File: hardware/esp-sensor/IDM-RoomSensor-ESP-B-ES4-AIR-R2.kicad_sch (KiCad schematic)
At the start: 115 parts, among them J1 MX205R / 43 TEMP / 42 +6-32V 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, J2 1-2834011-4 / RS485 A / B / C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, J3 TYPE-C-31-M-12, J4 EXPANSION / LED_EN / RELAY, J5 MX205R PUSH-IN / 3V3 / 1-WIRE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, J6 MX205R PUSH-IN / 3V3 / 1-WIRE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, J7 MX205R PUSH-IN / CONTACT1 / C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, J8 MX205R PUSH-IN / 0-10V IN / G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, J9 MX205R PUSH-IN / COM / NO / NC, K1 HFD4/5 5V DPDT signal relay, Q1 2N7002 60V VIN LED switch, Q2 2N7002 relay driver, SW1 RESET, SW2 BOOT, SW3 RS485 TERM ON/OFF, SW4 SERVICE / IDENTIFY, U1 LMR36510ADDAR 24V-to-5V, U10 BMP390, U11 AP2112K-3.3TRG1 AIR RAIL, U2 AP2112K-3.3TRG1, U3 ESP32-C6-WROOM-1-N16 (pins pe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, U4 SHT45-AD1B-R2, U5 MCP4725A0T-E/CH, U6 OPA197IDBVR, U7 CA-IS3092W, U8 SCD41-D-R1, U9 SGP41-D-R4

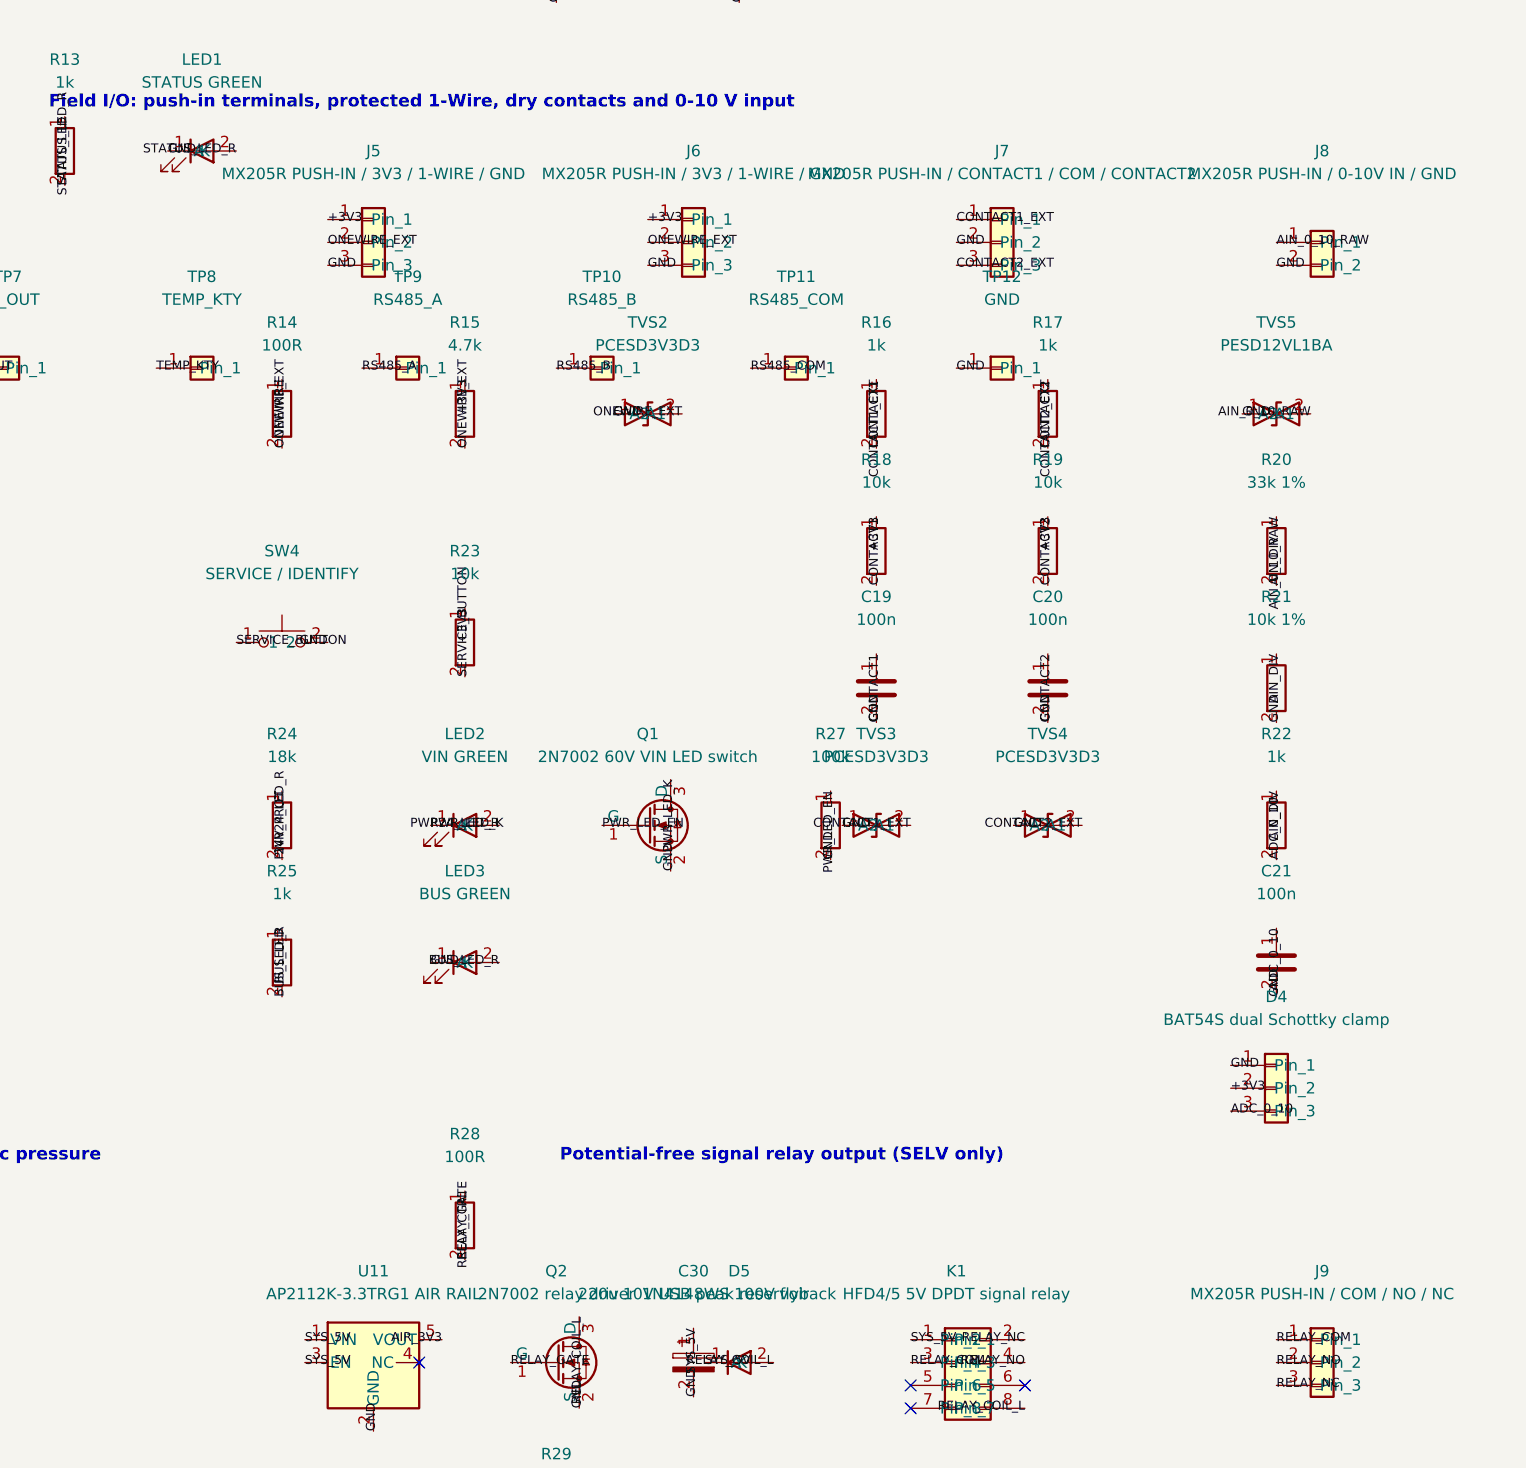
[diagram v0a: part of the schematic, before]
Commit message: Replace unavailable B-ES4 R2 terminals
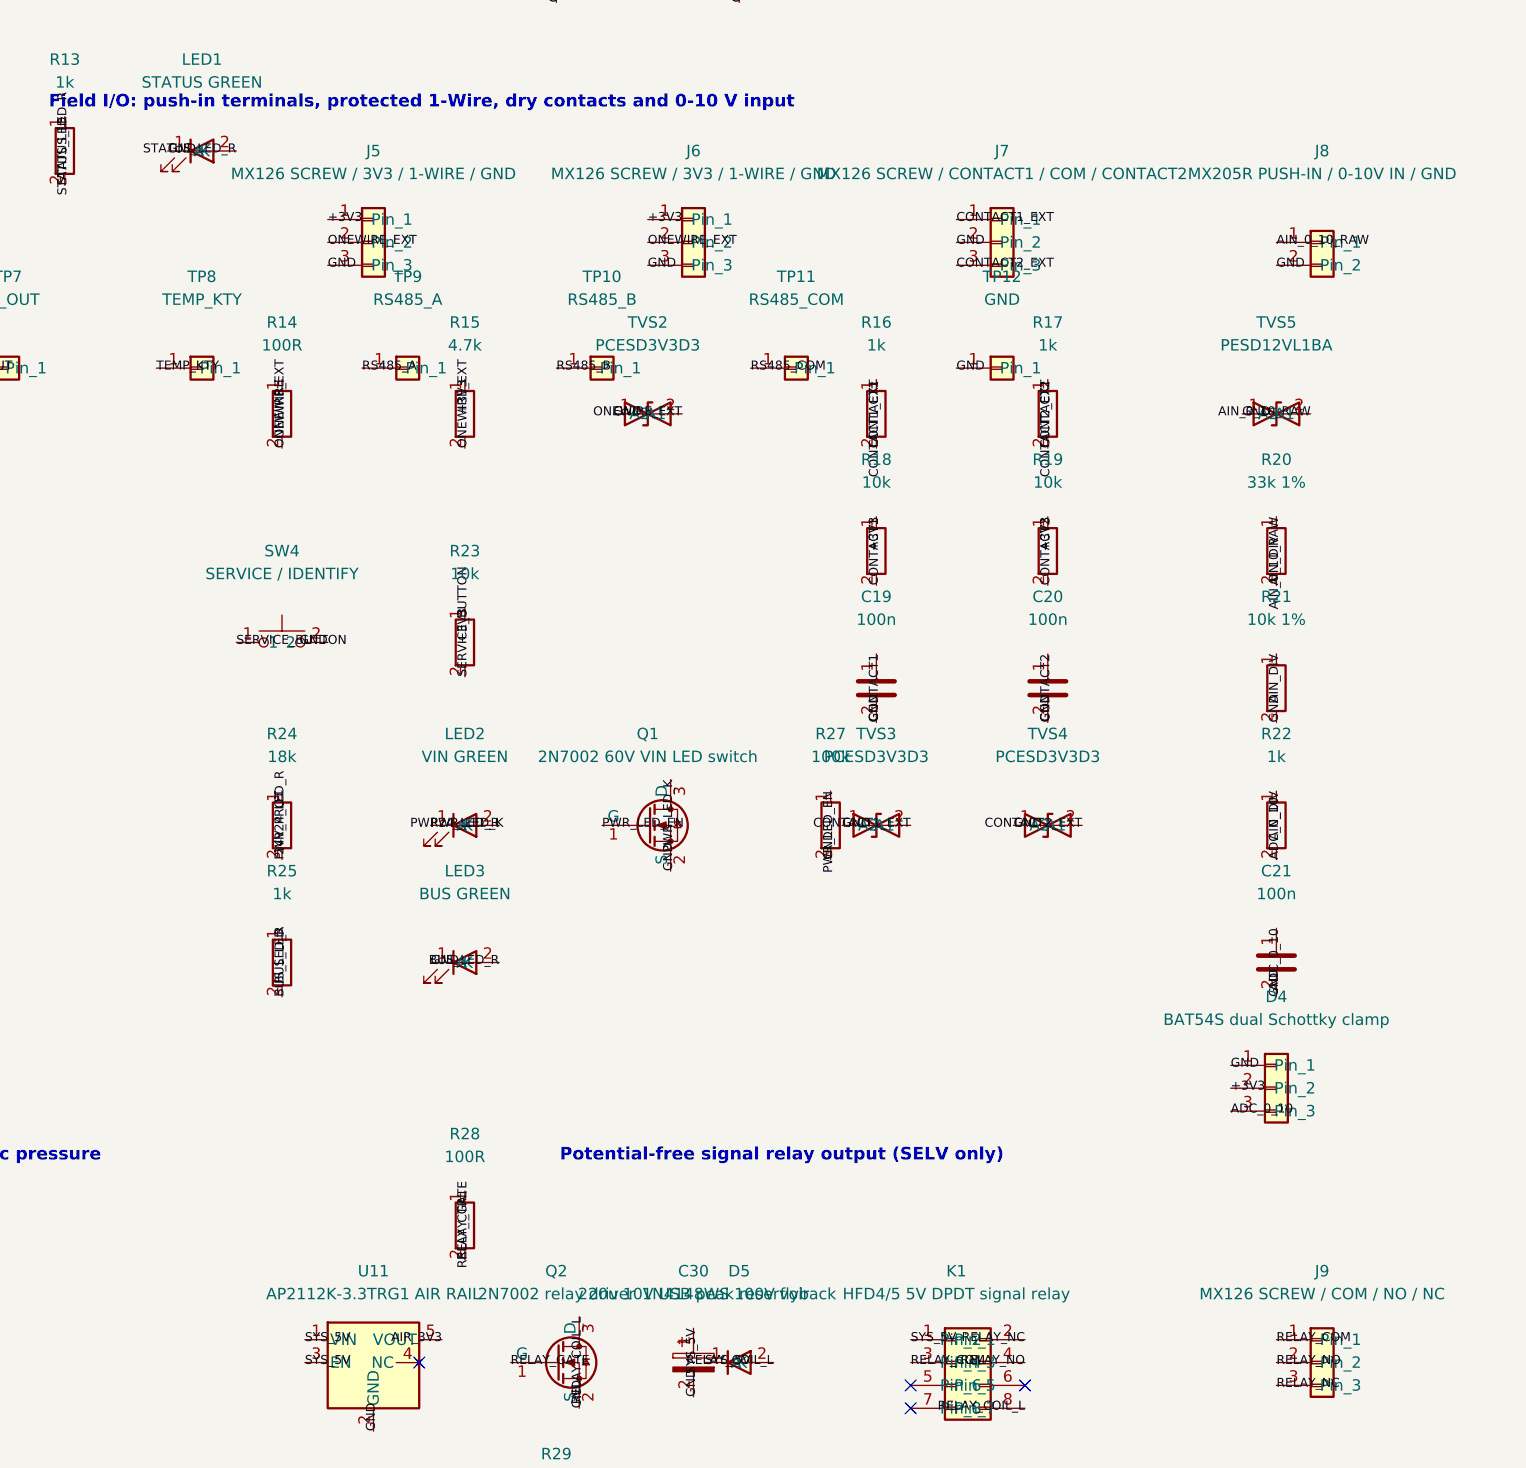
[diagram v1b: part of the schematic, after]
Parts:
- J5, J6: value MX205R PUSH-IN / 3V3 / 1-WIRE / GND -> MX126 SCREW / 3V3 / 1-WIRE / GND
- J7: value MX205R PUSH-IN / CONTACT1 / COM / CONTACT2 -> MX126 SCREW / CONTACT1 / COM / CONTACT2
- J9: value MX205R PUSH-IN / COM / NO / NC -> MX126 SCREW / COM / NO / NC
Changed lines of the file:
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@@
       (effects (font (size 1.27 1.27)))
     )
-    (property "Value" "MX205R PUSH-IN / 3V3 / 1-WIRE / GND" (at 214.63 182.88 0)
+    (property "Value" "MX126 SCREW / 3V3 / 1-WIRE / GND" (at 214.63 182.88 0)
       (effects (font (size 1.27 1.27)))
     )
@@
       (effects (font (size 1.27 1.27)) hide)
     )
-    (property "Datasheet" "https://www.lcsc.com/product-detail/C7471335.html" (at 214.63 185.42000000000002 0)
+    (property "Datasheet" "https://www.lcsc.com/product-detail/C5188435.html" (at 214.63 185.42000000000002 0)
       (effects (font (size 1.27 1.27)) hide)
     )
@@
       (effects (font (size 1.27 1.27)))
     )
-    (property "Value" "MX205R PUSH-IN / 3V3 / 1-WIRE / GND" (at 250.19 182.88 0)
+    (property "Value" "MX126 SCREW / 3V3 / 1-WIRE / GND" (at 250.19 182.88 0)
       (effects (font (size 1.27 1.27)))
     )
@@
       (effects (font (size 1.27 1.27)) hide)
     )
-    (property "Datasheet" "https://www.lcsc.com/product-detail/C7471335.html" (at 250.19 185.42000000000002 0)
+    (property "Datasheet" "https://www.lcsc.com/product-detail/C5188435.html" (at 250.19 185.42000000000002 0)
       (effects (font (size 1.27 1.27)) hide)
     )
@@
       (effects (font (size 1.27 1.27)))
     )
-    (property "Value" "MX205R PUSH-IN / CONTACT1 / COM / CONTACT2" (at 284.48 182.88 0)
+    (property "Value" "MX126 SCREW / CONTACT1 / COM / CONTACT2" (at 284.48 182.88 0)
       (effects (font (size 1.27 1.27)))
     )
@@
       (effects (font (size 1.27 1.27)) hide)
     )
-    (property "Datasheet" "https://www.lcsc.com/product-detail/C7471335.html" (at 284.48 185.42000000000002 0)
+    (property "Datasheet" "https://www.lcsc.com/product-detail/C5188435.html" (at 284.48 185.42000000000002 0)
       (effects (font (size 1.27 1.27)) hide)
     )
@@
       (effects (font (size 1.27 1.27)))
     )
-    (property "Value" "MX205R PUSH-IN / COM / NO / NC" (at 320.04 307.34 0)
+    (property "Value" "MX126 SCREW / COM / NO / NC" (at 320.04 307.34 0)
       (effects (font (size 1.27 1.27)))
     )
@@
       (effects (font (size 1.27 1.27)) hide)
     )
-    (property "Datasheet" "https://www.lcsc.com/product-detail/C7471335.html" (at 320.04 309.87999999999994 0)
-      (effects (font (size 1.27 1.27)) hide)
-    )
+    (property "Datasheet" "https://www.lcsc.com/product-detail/C5188435.html" (at 320.04 309.87999999999994 0)
+      (effects (font (size 1.27 1.27)) hide)
+    )

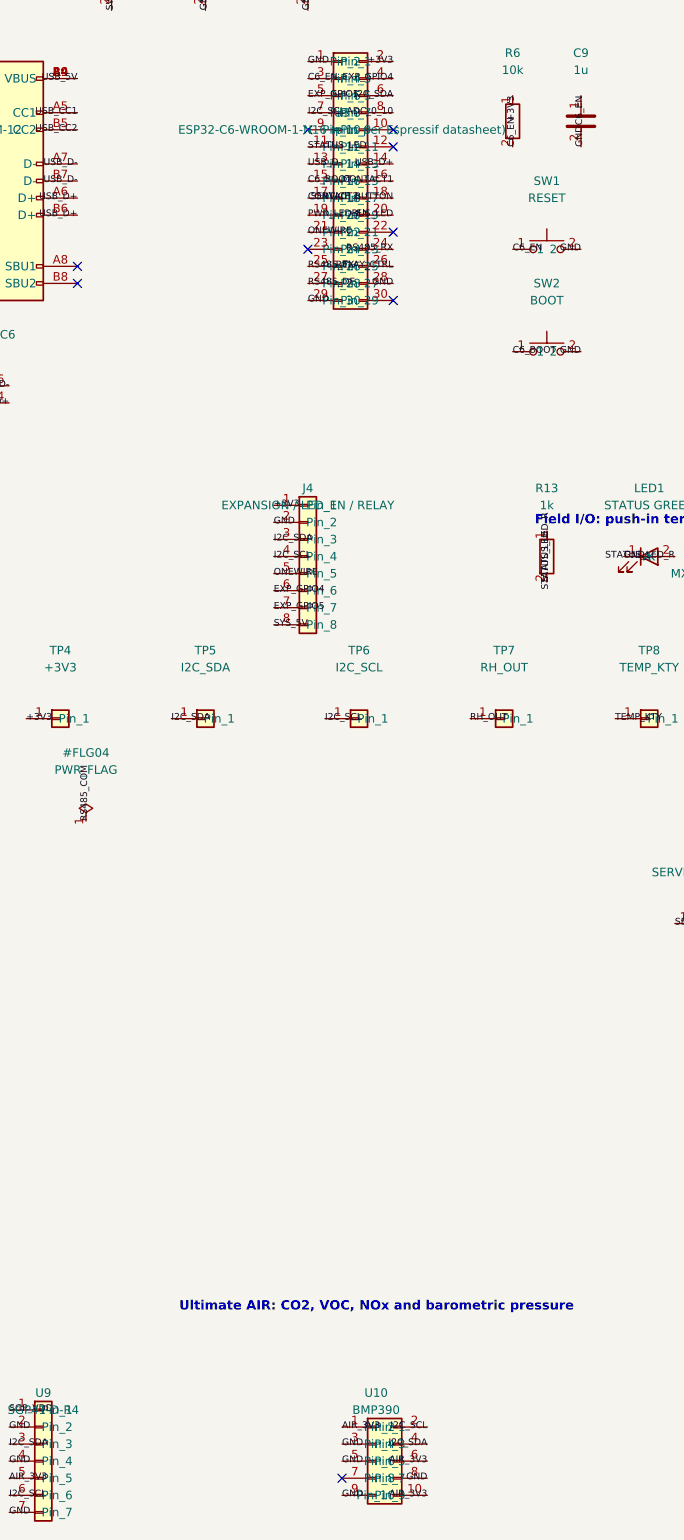
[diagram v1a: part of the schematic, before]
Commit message: Use stocked ESP32-C6 N8 and BMP388 for B-ES4 R2
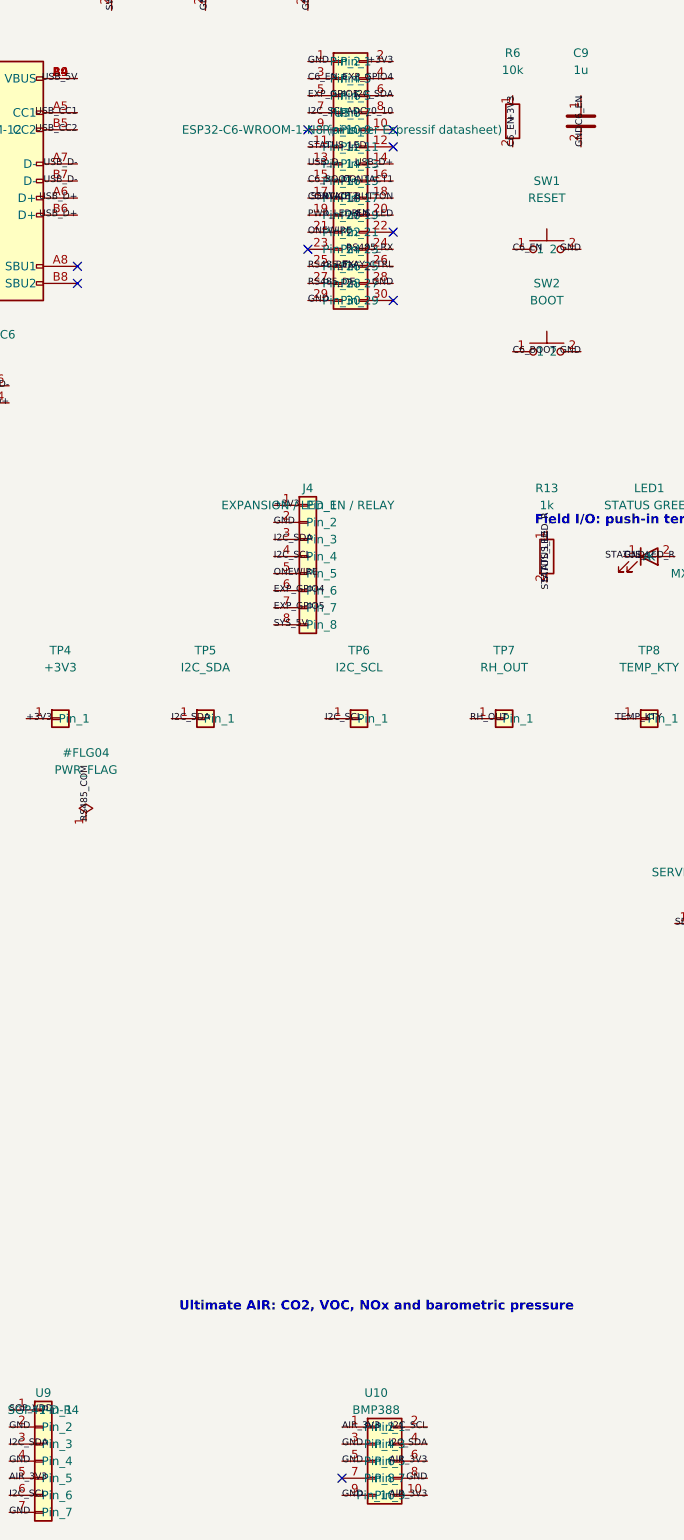
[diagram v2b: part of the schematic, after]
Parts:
- U10: value BMP390 -> BMP388
- U3: value ESP32-C6-WROOM-1-N16 (pins per Espressif datasheet) -> ESP32-C6-WROOM-1-N8 (pins per Espressif datasheet)
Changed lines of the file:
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@@
     (company "IDM Smart Climate Platform")
     (comment 1 "ENGINEERING SAMPLE - BENCH VALIDATION REQUIRED BEFORE IDM CONNECTION")
-    (comment 2 "ESP32-C6-N16; USB-C; 6-32 VDC; switchable LEDs; dry relay")
-    (comment 3 "SHT45 + SCD41 + SGP41 + BMP390 indoor-air sensing")
+    (comment 2 "ESP32-C6-N8; USB-C; 6-32 VDC; switchable LEDs; dry relay")
+    (comment 3 "SHT45 + SCD41 + SGP41 + BMP388 indoor-air sensing")
   )
   (no_connect (at 185.42 58.42))
@@
       (effects (font (size 1.27 1.27)))
     )
-    (property "Value" "ESP32-C6-WROOM-1-N16 (pins per Espressif datasheet)" (at 149.86 116.84000000000002 0)
+    (property "Value" "ESP32-C6-WROOM-1-N8 (pins per Espressif datasheet)" (at 149.86 116.84000000000002 0)
       (effects (font (size 1.27 1.27)))
     )
@@
       (effects (font (size 1.27 1.27)))
     )
-    (property "Value" "BMP390" (at 154.94 307.34 0)
+    (property "Value" "BMP388" (at 154.94 307.34 0)
       (effects (font (size 1.27 1.27)))
     )
@@
       (effects (font (size 1.27 1.27)) hide)
     )
-    (property "Datasheet" "https://www.bosch-sensortec.com/products/environmental-sensors/pressure-sensors/bmp390/" (at 154.94 309.87999999999994 0)
+    (property "Datasheet" "https://www.bosch-sensortec.com/products/environmental-sensors/pressure-sensors/bmp388/" (at 154.94 309.87999999999994 0)
       (effects (font (size 1.27 1.27)) hide)
     )
